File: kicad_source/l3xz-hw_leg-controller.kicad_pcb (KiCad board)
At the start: 2 copper layers, 178 x 29 mm, 16 parts, among them CN1 ARDUINO_NANO_33, U8 MCP2515, U9 SN65HVD232, Y1 16MHz

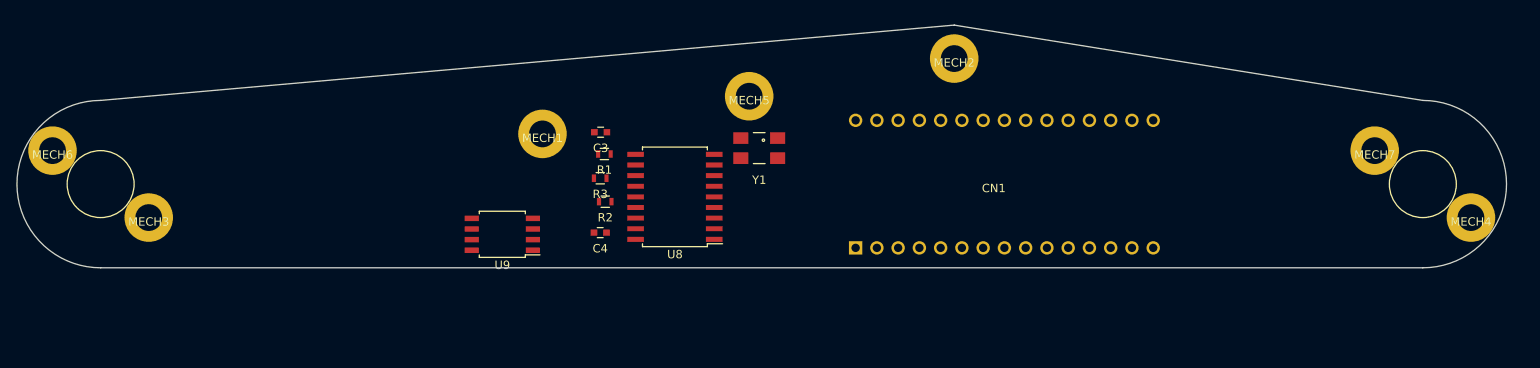
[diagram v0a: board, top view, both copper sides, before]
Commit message: added rotary encoder, led and switch
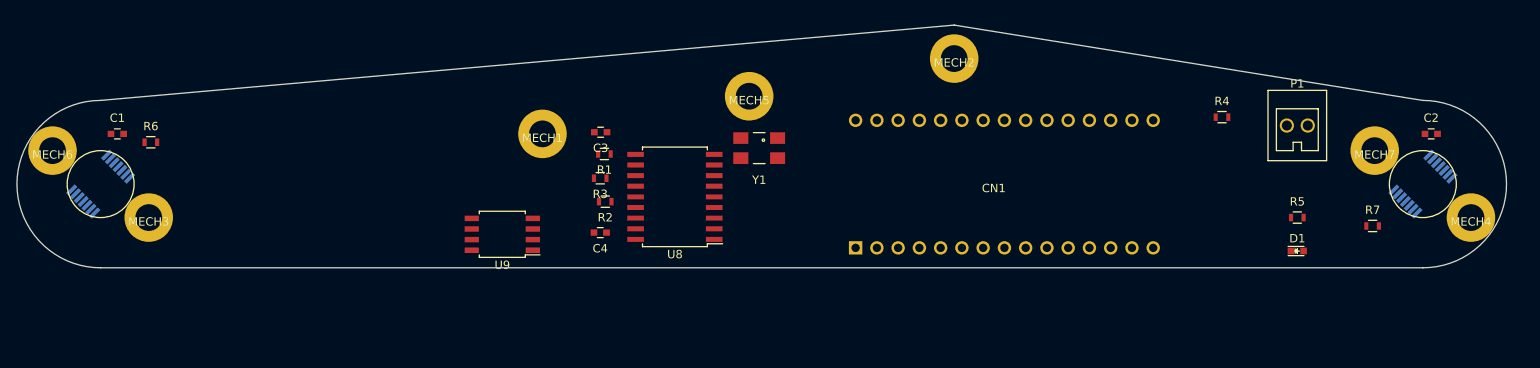
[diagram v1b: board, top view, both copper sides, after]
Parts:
- added C1: 100nF, capacitors:C_0603, F.Cu at (52.0, 84.0)
- added C2: 100nF, capacitors:C_0603, F.Cu at (209.0, 84.0)
- added D1: Led_Small, LEDs:LED_0603, F.Cu at (193.0, 98.0)
- added P1: CONN_01X02, CON_wuerth:WR-TBL_691382000002, F.Cu at (193.0, 83.0)
- added R4: 10k, resistors:R_0603, F.Cu at (184.0, 82.0)
- added R5: 10k, resistors:R_0603, F.Cu at (193.0, 94.0)
- added R6: 10k, resistors:R_0603, F.Cu at (56.0, 85.0)
- added R7: 10k, resistors:R_0603, F.Cu at (202.0, 95.0)
- added U1: AS5048A, SSOP:TSSOP-14_4.4x5mm_Pitch0.65mm, B.Cu at (50.0, 90.0)
- added U2: AS5048A, SSOP:TSSOP-14_4.4x5mm_Pitch0.65mm, B.Cu at (208.0, 90.0)
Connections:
- CN1 pad 20: (no net) -> /LED
- CN1 pad 22: (no net) -> AS5048_1_CS
- CN1 pad 23: (no net) -> AS5048_2_CS
- CN1 pad 24: (no net) -> /BUMPER

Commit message: made first draft for layout
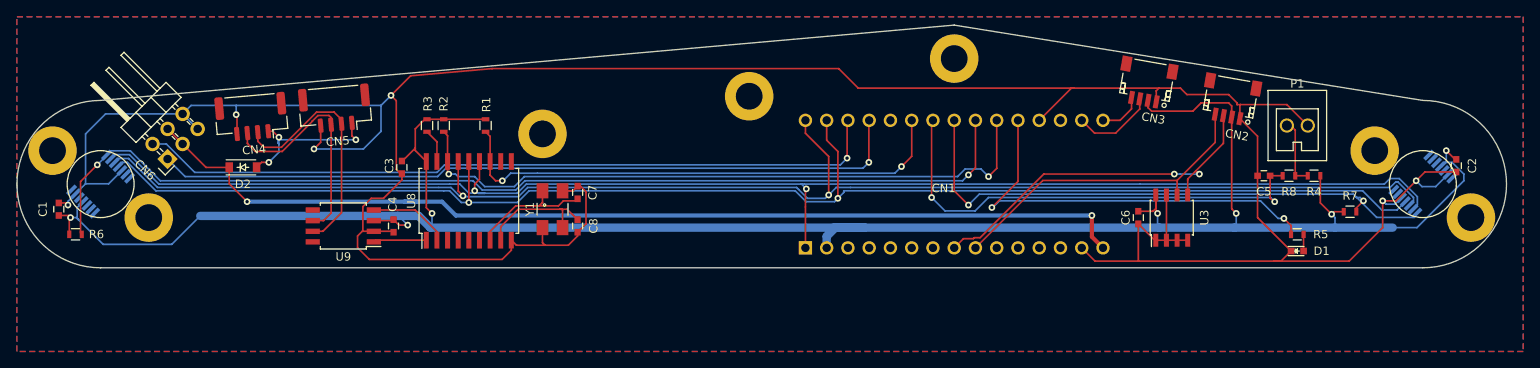
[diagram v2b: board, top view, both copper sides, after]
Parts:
- added C5: 100nF, capacitors:C_0603, F.Cu at (189.0, 89.0)
- added C6: 100nF, capacitors:C_0603, F.Cu at (174.0, 94.0)
- added C7: 10pF, capacitors:C_0603, F.Cu at (107.0, 91.0)
- added C8: 10pF, capacitors:C_0603, F.Cu at (107.0, 95.0)
- added CN2: SM04B-SRSS-TB, connectors_JST_SH:Connectors_JST_SM04B-SRSS-TB, F.Cu at (185.0, 80.0)
- added CN3: SM04B-SRSS-TB, connectors_JST_SH:Connectors_JST_SM04B-SRSS-TB, F.Cu at (175.0, 78.0)
- added CN4: GH_SM04B-GHS-TB, Connector_JST:JST_GH_SM04B-GHS-TB_1x04-1MP_P1.25mm_Horizontal, F.Cu at (68.0, 82.0)
- added CN5: GH_SM04B-GHS-TB, Connector_JST:JST_GH_SM04B-GHS-TB_1x04-1MP_P1.25mm_Horizontal, F.Cu at (78.0, 81.0)
- added CN6: CONN_02X03, pin_headers:Pin_Header_Angled_2x03, F.Cu at (58.0, 87.0)
- added D2: DNI, diodes:SOD-123, F.Cu at (67.0, 88.0)
- added R8: 1k, resistors:R_0603, F.Cu at (192.0, 89.0)
- added U3: 24LC64, SOIC:SOIC-8_3.9x4.9mm_Pitch1.27mm, F.Cu at (178.0, 94.0)
- moved Y1 25.8 mm to (104.0, 93.0), turned to 270 degrees
- moved C4 24.7 mm to (85.0, 95.0), turned to 270 degrees
- moved U8 24.6 mm to (94.0, 92.0), turned to 90 degrees
- moved C3 24.1 mm to (86.0, 88.0), turned to 270 degrees
- moved R3 21.6 mm to (89.0, 83.0), turned to 270 degrees
- moved R2 21.3 mm to (91.0, 83.0), turned to 270 degrees
- moved U9 19.0 mm to (79.0, 95.0)
- moved R1 14.6 mm to (96.0, 83.0), turned to 270 degrees
- moved R6 14.2 mm to (47.0, 96.0)
- moved R4 13.0 mm to (195.0, 89.0), turned to 180 degrees
- moved C1 11.4 mm to (45.0, 93.0), turned to 90 degrees
- moved CN1 6.00 mm to (152.0, 90.0)
- moved C2 4.84 mm to (212.0, 87.8), turned to 270 degrees
- moved R7 3.19 mm to (199.3, 93.3)
- moved R5 2.00 mm to (193.0, 96.0)
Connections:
- CN1 pad 15: (no net) -> +5V
- CN1 pad 16: (no net) -> SER_RX
- CN1 pad 17: (no net) -> SER_TX
- CN1 pad 27: (no net) -> /SERVO1
- CN1 pad 28: (no net) -> /SERVO2
- CN1 pad 8: (no net) -> I2C_SDA
- CN1 pad 9: (no net) -> I2C_SCL
- P1 pad 1: /BUMPER -> Net-(P1-Pad1)
- R4 pad 2: /BUMPER -> Net-(P1-Pad1)
- U9 pad 6: (no net) -> /MCP2515/CANL
- U9 pad 7: (no net) -> /MCP2515/CANH
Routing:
- net GND: track 0.00 -> 360.5 mm, vias 0 -> 6
- net +3V3: track 0.00 -> 265.8 mm, vias 0 -> 7
- net MISO: track 0.00 -> 175.5 mm, vias 0 -> 2
- net SCK: track 0.00 -> 174.9 mm, vias 0 -> 2
- net MOSI: track 0.00 -> 173.9 mm, vias 0 -> 2
- net AS5048_1_CS: track 0.00 -> 123.6 mm, vias 0 -> 2
- net +5V: track 0.00 -> 121.8 mm, vias 0 -> 2
- net /SERVO1: track 0.00 -> 90.4 mm, vias 0 -> 1
- net /SERVO2: track 0.00 -> 89.7 mm, vias 0 -> 1
- net MCP2515_CS: track 0.00 -> 78.8 mm, vias 0 -> 2
- net AS5048_2_CS: track 0.00 -> 69.1 mm, vias 0 -> 2
- net MCP2515_INT: track 0.00 -> 61.6 mm, vias 0 -> 2
- net /BUMPER: track 0.00 -> 56.7 mm, vias 0 -> 2
- net /LED: track 0.00 -> 50.1 mm, vias 0 -> 2
- net I2C_SDA: track 0.00 -> 44.8 mm, vias 0 -> 2
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- added copper zone on B.Cu, net GND
- added copper zone on F.Cu, net GND

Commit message: added pull up to i2c, serial resistor to servo
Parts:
- added R10: 10k, resistors:R_0603, F.Cu at (177.8, 86.3)
- added R11: 100R, resistors:R_0603, F.Cu at (60.9, 90.2)
- added R12: 100R, resistors:R_0603, F.Cu at (60.9, 88.5)
- added R9: 10k, resistors:R_0603, F.Cu at (179.6, 86.3)
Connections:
- CN6 pad 1: /SERVO1 -> /SERVO1_R
- CN6 pad 2: /SERVO2 -> /SERVO2_R
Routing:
- net /SERVO2_R: track 0.00 -> 7.63 mm
- net +3V3: track 265.8 -> 272.3 mm
- net /SERVO2: track 89.7 -> 84.0 mm, vias 1 -> 2
- net /SERVO1_R: track 0.00 -> 4.09 mm
- net /SERVO1: track 90.4 -> 86.8 mm, vias 1 -> 2
- net I2C_SDA: track 44.8 -> 46.8 mm
- net I2C_SCL: track 39.0 -> 40.1 mm

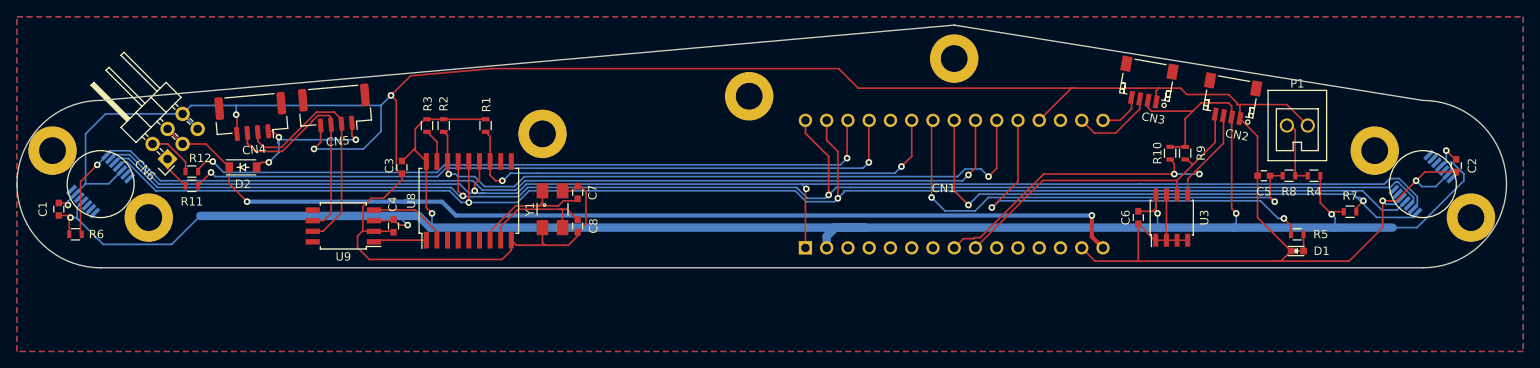
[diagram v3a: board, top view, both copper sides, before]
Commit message: updated connectors, added power input
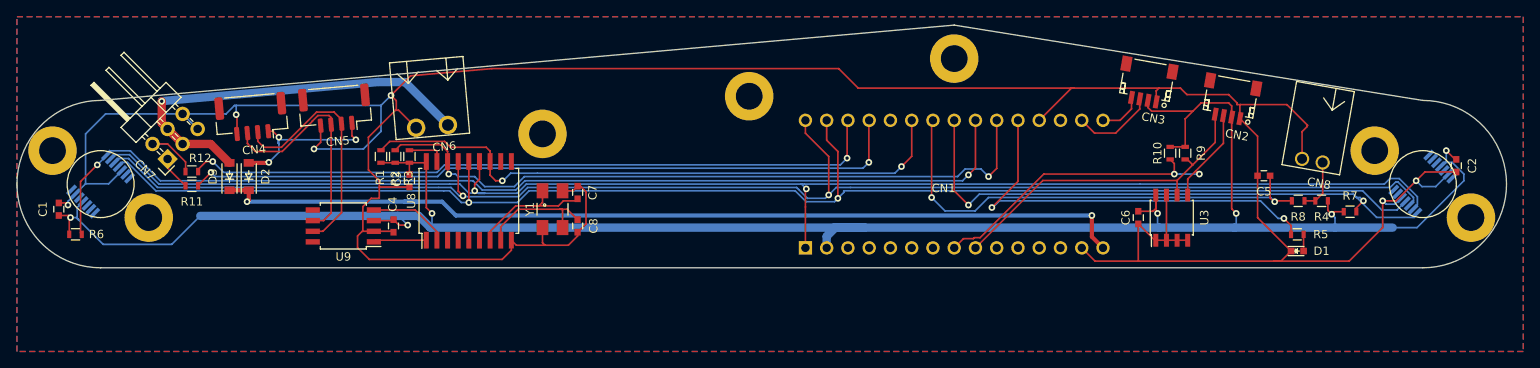
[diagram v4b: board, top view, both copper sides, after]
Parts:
- removed P1: CONN_01X02, CON_wuerth:WR-TBL_691382000002
- added CN6: 691322310002, CON_wuerth:WR-TBL_691322310002, F.Cu at (89.6, 83.1)
- added CN8: 691382010002, CON_wuerth:WR-TBL_691382010002, F.Cu at (194.8, 87.2)
- added D3: DNI, diodes:SOD-123, F.Cu at (65.4, 89.1)
- moved R1 13.0 mm to (83.5, 86.7), turned to 90 degrees
- moved R2 6.88 mm to (85.2, 86.7), turned to 90 degrees
- moved R3 4.25 mm to (86.9, 86.7), turned to 90 degrees
- moved R8 3.20 mm to (193.1, 92.0)
- moved R4 3.13 mm to (195.9, 92.0)
- moved C3 1.84 mm to (86.9, 89.6)
- moved D2 1.30 mm to (67.7, 89.1), turned to 90 degrees
- renumbered CN6 to CN7
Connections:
- net Net-(P1-Pad1) renamed /BUMPER_R
- CN1 pad 15: +5V -> +BATT
- CN7 pad 3: +5V -> /V_IN
- CN7 pad 4: +5V -> /V_IN
- D2 pad 1: +5V -> +BATT
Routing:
- net +5V: track 121.8 -> 0.00 mm, vias 2 -> 0
- net +BATT: track 0.00 -> 111.3 mm, vias 0 -> 2
- net /V_IN: track 0.00 -> 49.1 mm, vias 0 -> 1
- net +3V3: track 272.3 -> 260.2 mm
- net GND: track 360.5 -> 372.0 mm
- net MCP2515_INT: track 61.6 -> 73.0 mm
- net MCP2515_CS: track 78.8 -> 83.2 mm
- net /BUMPER_R: track 8.18 -> 6.25 mm
- net /MCP2515/CANVCC: track 18.8 -> 20.4 mm
- net /BUMPER: track 56.7 -> 57.3 mm
- net Net-(R3-Pad2): track 4.04 -> 4.55 mm

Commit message: added additional leds, input measurement buffer capacitors
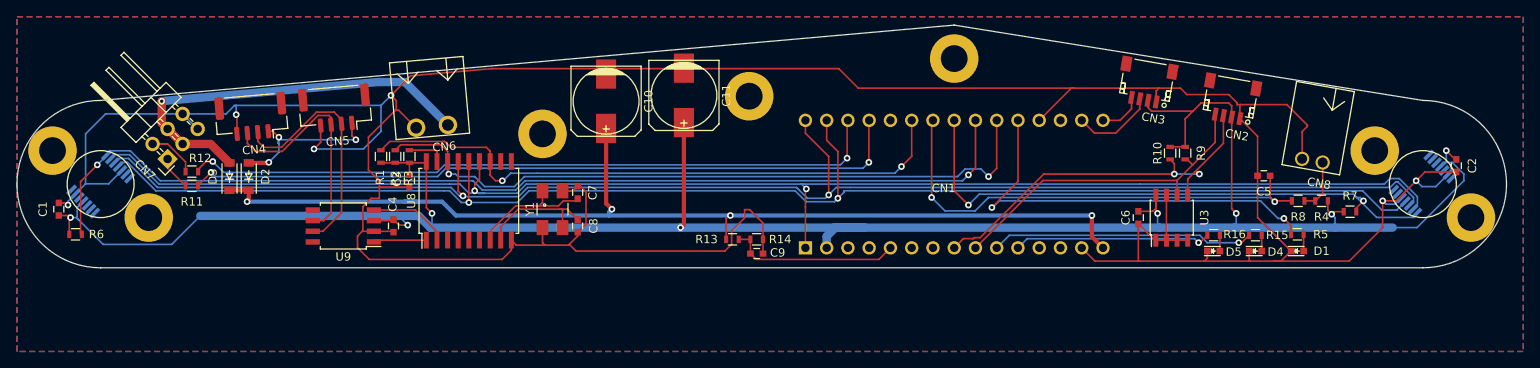
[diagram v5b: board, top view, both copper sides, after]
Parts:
- added C10: 100uF 25V, capacitors:c_elec_8x10, F.Cu at (110.4, 80.1)
- added C11: 100uF 25V, capacitors:c_elec_8x10, F.Cu at (119.7, 79.4)
- added C9: 100nF, capacitors:C_0603, F.Cu at (128.4, 98.3)
- added D4: Led_Small, LEDs:LED_0603, F.Cu at (188.0, 98.0)
- added D5: Led_Small, LEDs:LED_0603, F.Cu at (183.0, 98.0)
- added R13: 10k, resistors:R_0603, F.Cu at (125.5, 96.6)
- added R14: 1k, resistors:R_0603, F.Cu at (128.4, 96.6)
- added R15: 10k, resistors:R_0603, F.Cu at (188.0, 96.1)
- added R16: 10k, resistors:R_0603, F.Cu at (183.0, 96.1)
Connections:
- net /LED renamed /LED1
- net Net-(D1-Pad2) renamed /LED1_R
- CN1 pad 10: (no net) -> /LED3
- CN1 pad 11: (no net) -> /LED2
- CN1 pad 5: (no net) -> /+BATT_MEAS
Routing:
- net GND: track 372.0 -> 405.9 mm
- net /LED3: track 0.00 -> 31.5 mm, vias 0 -> 1
- net /LED2: track 0.00 -> 23.7 mm, vias 0 -> 1
- net /+BATT_MEAS: track 0.00 -> 20.7 mm
- net +BATT: track 111.3 -> 125.3 mm, vias 2 -> 4
- net +3V3: track 260.2 -> 272.9 mm, vias 7 -> 8
- net /LED3_R: track 0.00 -> 1.90 mm
- net /LED2_R: track 0.00 -> 1.90 mm

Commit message: added labels, beautified layout
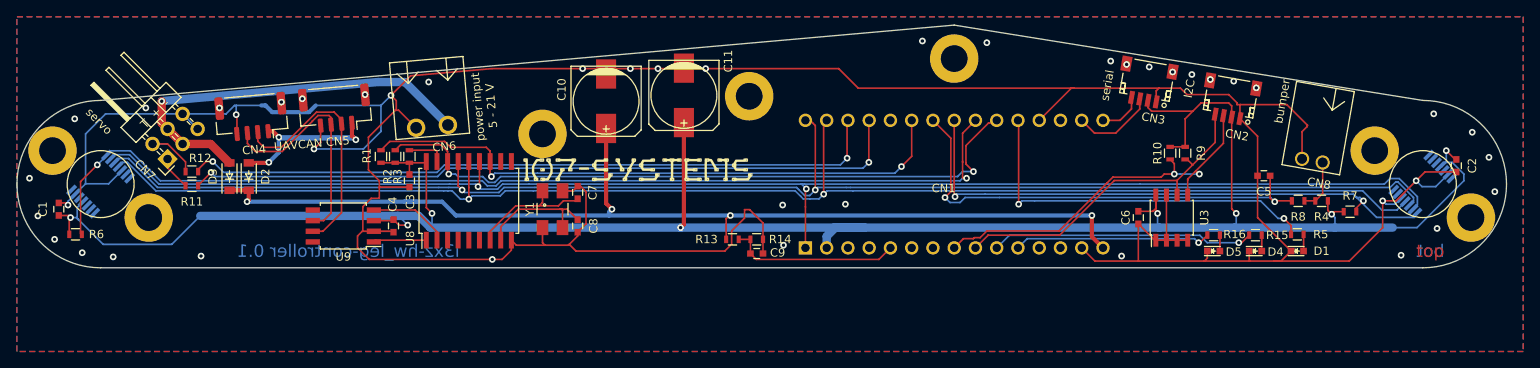
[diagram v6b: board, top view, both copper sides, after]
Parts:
- added L1: Label, labels:107systems_logo_small, F.Cu at (114.2, 88.3)
- added L2: Label, labels:107-systems_logo_big, B.Cu at (145.9, 90.2)
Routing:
- net /MCP2515/CANVCC: track 20.4 -> 31.5 mm
- net /LED1: track 50.1 -> 45.0 mm
- net SCK: track 174.9 -> 172.3 mm
- net MISO: track 175.5 -> 173.1 mm
- net MOSI: track 173.9 -> 171.9 mm
- net MCP2515_CS: track 83.2 -> 81.7 mm
- net /BUMPER: track 57.3 -> 56.0 mm
- net GND: track 405.9 -> 406.6 mm, vias 6 -> 36
- net (no net): vias 0 -> 8
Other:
- board text added: "I2C"
- board text added: "T + -"
- board text added: "UAVCAN"
- board text added: "bot"
- board text added: "bumper"
- board text added: "l3xz-hw_leg-controller 0.1"
- board text added: "power input 5 - 21 V"
- board text added: "serial"
- board text added: "servo"
- board text added: "top"

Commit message: added alternative DIL package for MCP2515
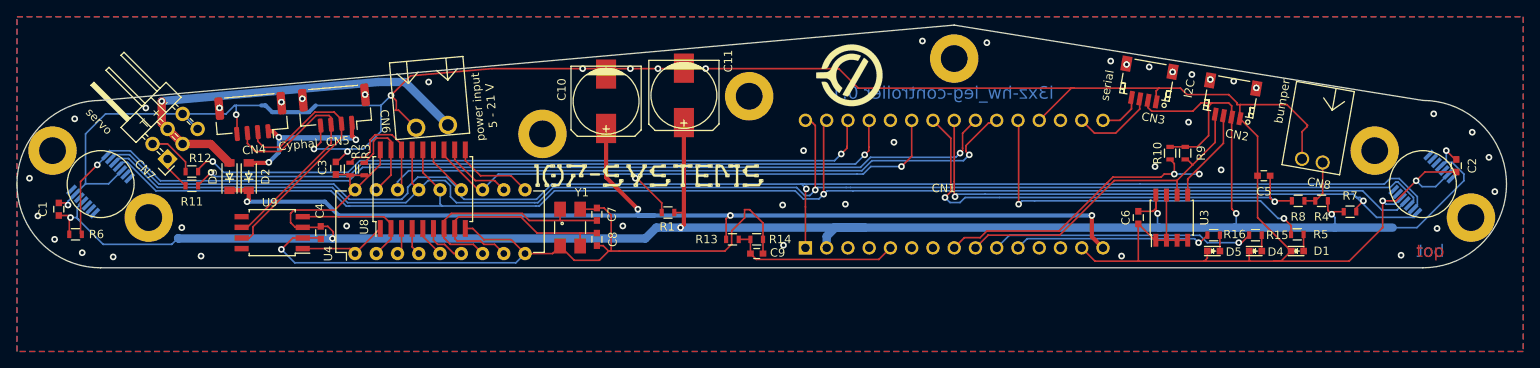
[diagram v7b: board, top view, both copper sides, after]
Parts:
- added L3: Label, labels:opencyphal_small, F.Cu at (139.5, 77.0)
- added U4: MCP2515, DIP:DIP-18_W7.62mm, F.Cu at (80.4, 98.3)
- moved R1 34.9 mm to (117.8, 93.4), turned to 180 degrees
- moved C3 8.93 mm to (78.1, 88.1), turned to 90 degrees
- moved C4 8.74 mm to (76.3, 95.8)
- moved U9 8.54 mm to (70.5, 95.8)
- moved U8 5.68 mm to (88.5, 90.6)
- moved R2 5.60 mm to (79.8, 88.2)
- moved R3 5.60 mm to (81.5, 88.2)
- moved C7 3.47 mm to (109.3, 93.6)
- moved Y1 3.04 mm to (106.1, 95.2)
- moved C8 2.80 mm to (109.3, 96.6)
- moved L1 1.48 mm to (115.5, 89.0)
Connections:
- net Net-(C7-Pad1) renamed /MCP2515/MCP2515_OSC2
- net Net-(C8-Pad1) renamed /MCP2515/MCP2515_OSC1
- net Net-(R3-Pad2) renamed /MCP2515/MCP2515_RESET
- U8 pad 10: (no net) -> /MCP2515/MCP2515_RX1BUF
- U8 pad 11: (no net) -> /MCP2515/MCP2515_RX0BUF
- U8 pad 3: (no net) -> /MCP2515/MCP2515_SOF
- U8 pad 4: (no net) -> /MCP2515/MCP2515_TX0RTS
- U8 pad 5: (no net) -> /MCP2515/MCP2515_TX1RTS
- U8 pad 6: (no net) -> /MCP2515/MCP2515_TX2RTS
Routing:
- net /MCP2515/MCP2515_OSC1: track 14.6 -> 28.3 mm
- net /MCP2515/MCP2515_OSC2: track 15.1 -> 27.6 mm
- net +3V3: track 272.9 -> 283.3 mm, vias 8 -> 7
- net /MCP2515/MCP2515_RX1BUF: track 0.00 -> 9.87 mm
- net MCP2515_CS: track 81.7 -> 91.3 mm, vias 2 -> 1
- net /MCP2515/MCP2515_RX0BUF: track 0.00 -> 8.55 mm
- net /MCP2515/MCP2515_RESET: track 4.55 -> 11.9 mm
- net SCK: track 172.3 -> 179.4 mm, vias 2 -> 1
- net MISO: track 173.1 -> 178.6 mm, vias 2 -> 1
- net /MCP2515/RXCAN: track 9.62 -> 15.0 mm
- net /MCP2515/MCP2515_TX2RTS: track 0.00 -> 5.19 mm
- net GND: track 406.6 -> 401.6 mm, vias 36 -> 45
- net /MCP2515/TXCAN: track 6.35 -> 10.7 mm
- net /MCP2515/CANH: track 29.0 -> 33.1 mm
- net /MCP2515/CANL: track 27.5 -> 31.5 mm
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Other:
- board text added: "Cyphal"
- board text removed: "UAVCAN"
